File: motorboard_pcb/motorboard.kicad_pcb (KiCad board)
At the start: 4 copper layers, 72 x 65.4 mm, 65 parts, among them J1 RJ45, J2 RJ45, J3 Conn_01x02_Pin, J4 BATT+, J6 THROTTLE, J7 BATT-, U1 XIAO-RP2350-SMD, U11 TLV76701DRVR, U2 TCAN1042HGVDQ1, U3 ISO7041FQDBQRQ1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

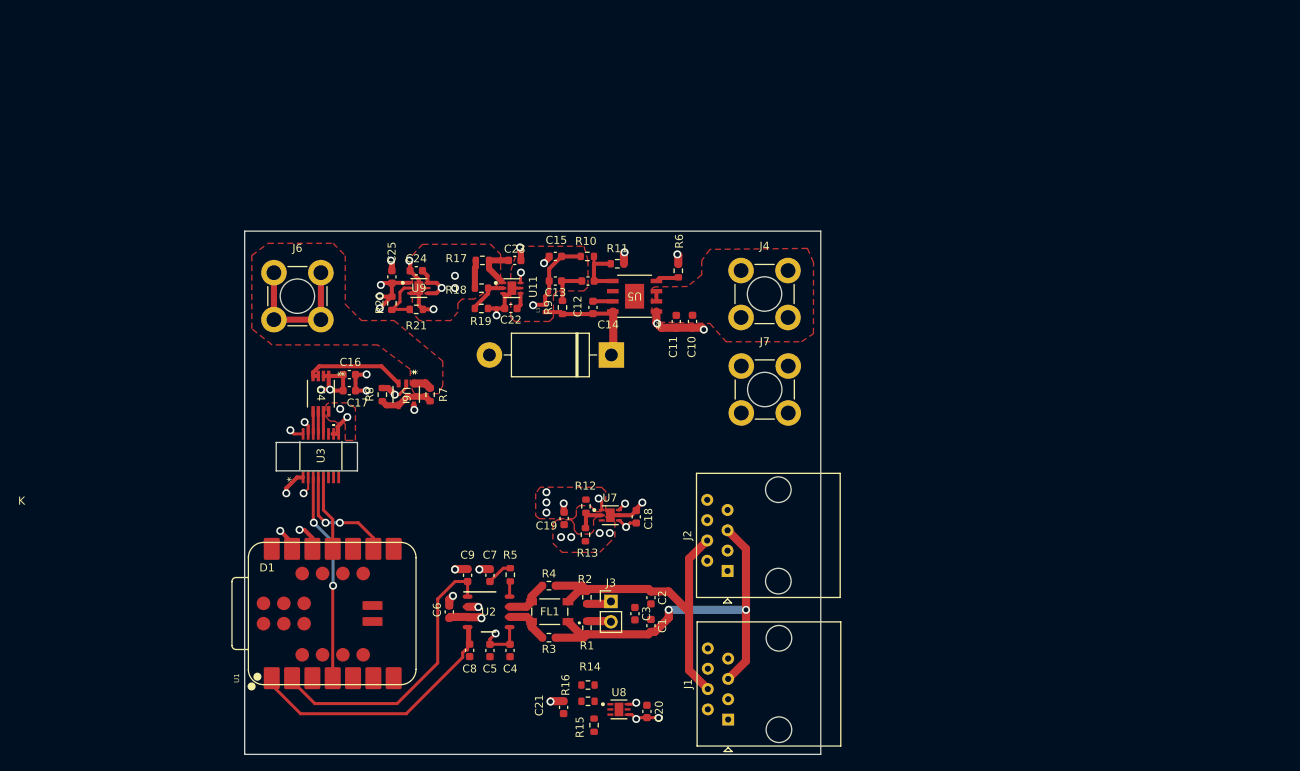
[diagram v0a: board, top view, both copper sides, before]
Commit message: layout finished, silkscreen finished, BOM finished
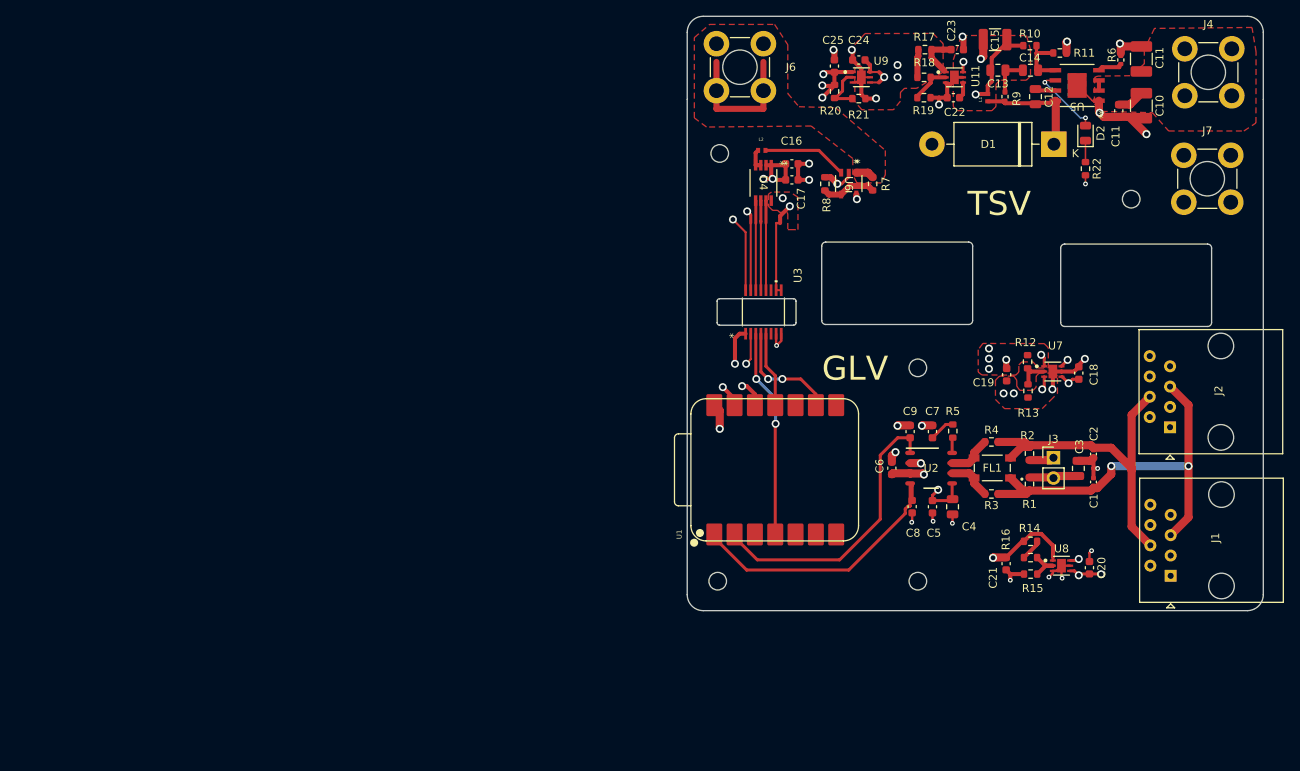
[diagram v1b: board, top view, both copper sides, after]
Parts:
- added C11: 2.2u, Capacitor_SMD:C_1210_3225Metric_Pad1.33x2.70mm_HandSolder, F.Cu at (164.5, 65.3)
- added D2: LED, LED_SMD:LED_0805_2012Metric, F.Cu at (157.6, 74.6)
- added G***: LOGO, Logo:mozee_logo, B.Cu at (124.4, 115.2)
- added H1: MountingHole_Pad, MountingHole:MountingHole_2.2mm_M2, F.Cu at (111.8, 77.2)
- added H2: MountingHole_Pad, MountingHole:MountingHole_2.2mm_M2, F.Cu at (136.6, 104.0)
- added H3: MountingHole_Pad, MountingHole:MountingHole_2.2mm_M2, F.Cu at (136.6, 130.6)
- added H3: MountingHole_Pad, MountingHole:MountingHole_2.2mm_M2, F.Cu at (111.6, 130.6)
- added H4: MountingHole_Pad, MountingHole:MountingHole_2.2mm_M2, F.Cu at (163.3, 82.9)
- added L2: LQW15AN47NG00D, LQW15AN47NG00D:INDC1005X60N, F.Cu at (117.1, 76.8)
- added R22: 16k, Resistor_SMD:R_0603_1608Metric, F.Cu at (157.6, 79.1)
- C1, C2: footprint Capacitor_SMD:C_0603_1608Metric -> Capacitor_SMD:C_0402_1005Metric
- C10: footprint Capacitor_SMD:C_0603_1608Metric -> Capacitor_SMD:C_1210_3225Metric_Pad1.33x2.70mm_HandSolder
- C12, C13, C14, C3, C4: footprint Capacitor_SMD:C_0603_1608Metric -> Capacitor_SMD:C_0805_2012Metric
- C15: footprint Capacitor_SMD:C_0603_1608Metric -> Capacitor_SMD:C_1210_3225Metric
- R12, R20: value 50k -> 49.9k
- R6: footprint Resistor_SMD:R_0603_1608Metric -> Resistor_SMD:R_0402_1005Metric
- R9: footprint Resistor_SMD:R_0603_1608Metric -> Resistor_SMD:R_0402_1005Metric_Pad0.72x0.64mm_HandSolder
- moved J6 62.3 mm to (114.4, 66.4)
- moved C10 62.3 mm to (164.5, 71.2)
- moved J4 62.0 mm to (172.9, 67.0)
- moved R20 61.3 mm to (126.2, 69.4), turned to 90 degrees
- moved C15 61.3 mm to (146.2, 62.9)
- moved C11 61.3 mm to (161.7, 71.8)
- moved C12 61.3 mm to (151.3, 70.1)
- moved C16 61.3 mm to (120.8, 78.5)
- moved R11 61.3 mm to (154.3, 64.6)
- moved R18 61.3 mm to (137.4, 67.6)
- moved R7 61.3 mm to (130.9, 81.0)
- moved C13 61.3 mm to (146.6, 66.8)
- moved C14 61.3 mm to (150.7, 66.8)
- moved C17 61.3 mm to (120.8, 80.5)
- moved C22 61.3 mm to (141.0, 70.2)
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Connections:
- C14 pad 2: Net-(U5-FB) -> Net-(D2-A)
- R10 pad 1: Net-(U5-FB) -> Net-(D2-A)
- R11 pad 2: Net-(U5-FB) -> Net-(D2-A)
- R12 pad 1: +3.3VL -> Net-(U7-FB)
- R12 pad 2: Net-(U7-FB) -> +3.3VL
- R20 pad 1: +3.3VH -> Net-(U9-FB)
- R20 pad 2: Net-(U9-FB) -> +3.3VH
- U1 pad 14: unconnected-(U1-5V-Pad14) -> +5VL
- U4 pad 3: /DAC_OUT -> Net-(U4-VFB)
- U4 pad 4: /DAC_OUT -> Net-(U4-VFB)
- U5 pad 5: Net-(U5-FB) -> Net-(D2-A)
- U5 pad 6: unconnected-(U5-PGOOD-Pad6) -> Net-(D2-A)
- U5 pad EPAD: (no net) -> GND2
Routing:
- net +5VL: track 22.8 -> 63.5 mm, vias 2 -> 3
- net GND2: track 46.3 -> 74.0 mm, vias 16 -> 17
- net GND: track 15.6 -> 42.7 mm, vias 11 -> 20
- net Net-(D2-A): track 0.00 -> 16.8 mm, vias 0 -> 2
- net Net-(U3-OUTB): track 2.82 -> 11.4 mm
- net Net-(U3-OUTC): track 2.82 -> 11.2 mm
- net Net-(U3-OUTA): track 2.82 -> 11.2 mm
- net +3.3VH: track 20.0 -> 27.7 mm
- net Net-(U5-FB): track 7.51 -> 0.00 mm
- net Net-(U8-FB): track 0.00 -> 4.90 mm
- net /TSV_Power/84VH: track 1.27 -> 4.68 mm
- net Net-(J3-Pin_2): track 3.03 -> 6.25 mm
- net Net-(R14-Pad2): track 0.00 -> 2.72 mm
- net Net-(D2-K): track 0.00 -> 2.68 mm
- net Net-(U4-VFB): track 0.00 -> 2.59 mm
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- added copper zone on B.Cu, net GND2
- added copper zone on In2.Cu, net GND2
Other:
- board size 72 x 65.4 mm -> 72 x 74.3 mm
- board text added: "GLV"
- board text added: "TSV"
